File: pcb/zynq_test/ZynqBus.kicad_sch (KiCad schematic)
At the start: 22 parts, among them U1 XC7Z020-2CLG400I

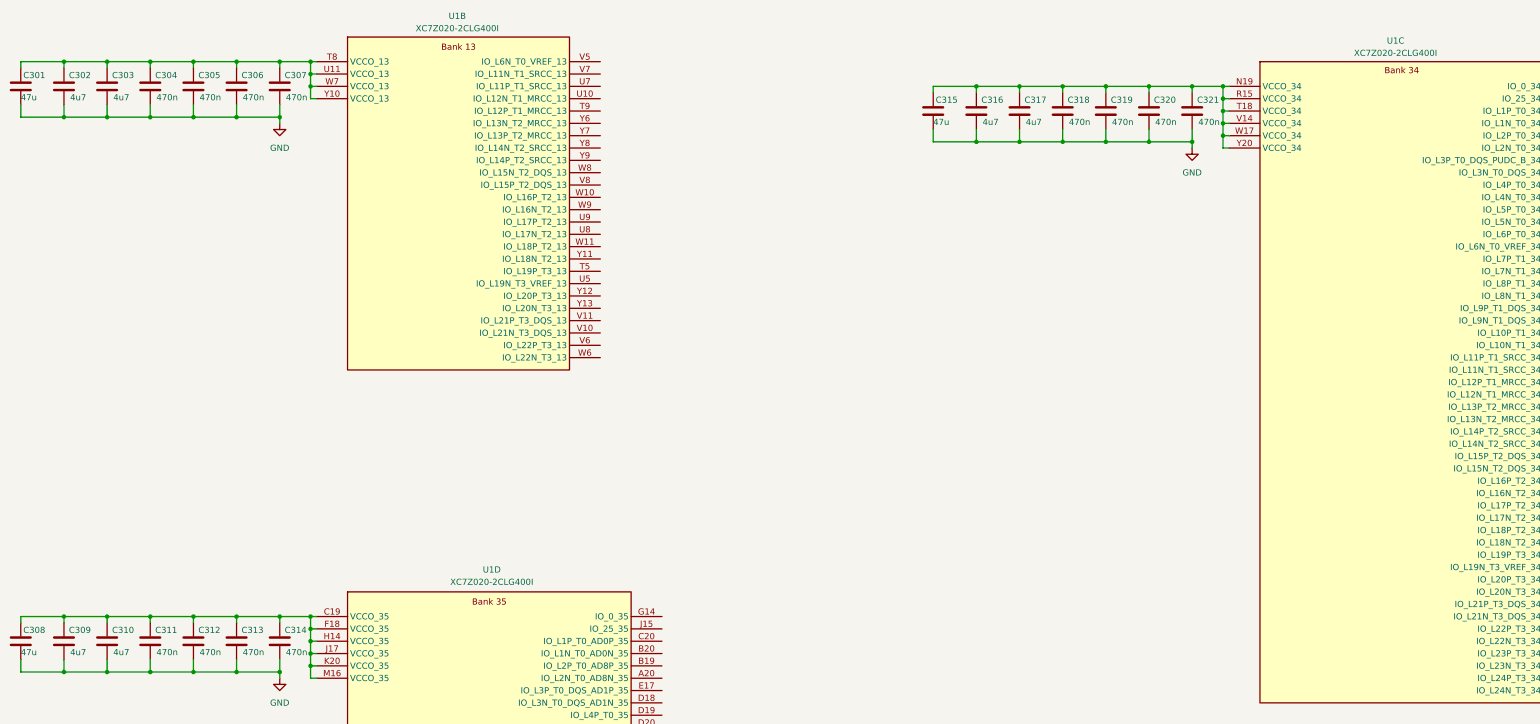
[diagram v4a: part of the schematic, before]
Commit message: Connected DDR3, cleaned up some thing
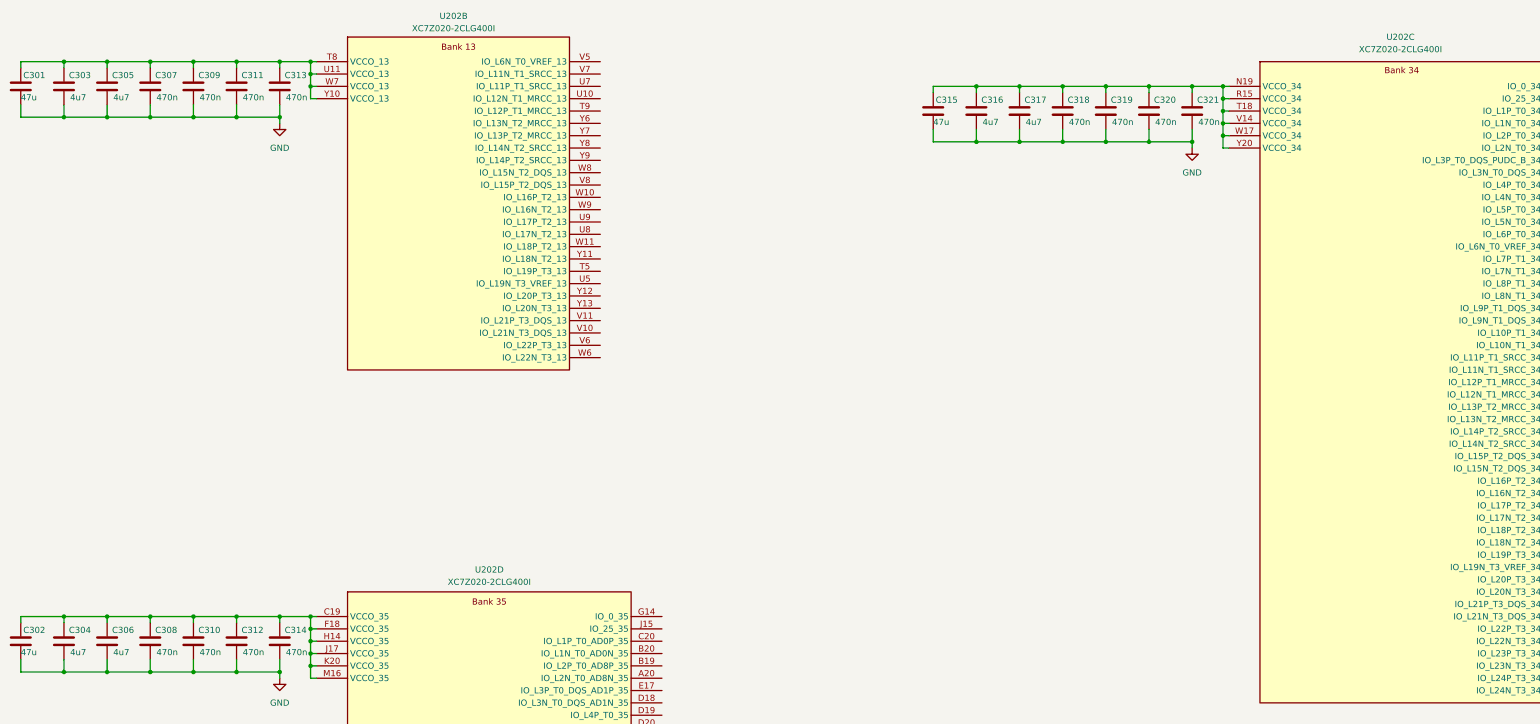
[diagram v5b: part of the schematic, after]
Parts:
- renumbered C308 to C302, C302 to C303, C309 to C304, C303 to C305, C310 to C306, C304 to C307, C311 to C308, C305 to C309, C312 to C310, C306 to C311, C313 to C312, C307 to C313, U1 to U202
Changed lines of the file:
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@@
 	(generator_version "9.0")
 	(paper "A3")
+	(title_block
+		(date "2025-09-06")
+		(rev "v1.0")
+	)
 	(junction
 		(at 240.03 44.45)
@@
 		(on_board yes)
 		(dnp no)
-		(property "Reference" "C313"
+		(property "Reference" "C312"
 			(at 61.976 145.034 0)
 			(effects
@@
 			(project "zynq_test"
 				(path "/0637578d-4ce5-4d31-b973-2de977269ea5/c459e1b5-5454-4a76-b5d2-e90b165c8789"
-					(reference "C313")
+					(reference "C312")
 					(unit 1)
 				)
@@
 		(on_board yes)
 		(dnp no)
-		(property "Reference" "C307"
+		(property "Reference" "C313"
 			(at 70.866 30.734 0)
 			(effects
@@
 			(project "zynq_test"
 				(path "/0637578d-4ce5-4d31-b973-2de977269ea5/c459e1b5-5454-4a76-b5d2-e90b165c8789"
-					(reference "C307")
+					(reference "C313")
 					(unit 1)
 				)
@@
 		(on_board yes)
 		(dnp no)
-		(property "Reference" "C303"
+		(property "Reference" "C305"
 			(at 35.306 30.734 0)
 			(effects
@@
 			(project "zynq_test"
 				(path "/0637578d-4ce5-4d31-b973-2de977269ea5/c459e1b5-5454-4a76-b5d2-e90b165c8789"
-					(reference "C303")
+					(reference "C305")
 					(unit 1)
 				)
@@
 	)
 	(symbol
-		(lib_name "XC7Z020-2CLG400I_2")
 		(lib_id "zynq:XC7Z020-2CLG400I")
 		(at 106.68 58.42 0)
@@
 		(on_board yes)
 		(dnp no)
-		(property "Reference" "U1"
-			(at 106.426 18.542 0)
+		(property "Reference" "U202"
+			(at 105.664 18.542 0)
 			(effects
 				(font
@@
 		)
 		(property "Value" "XC7Z020-2CLG400I"
-			(at 106.426 21.082 0)
+			(at 105.664 21.082 0)
 			(effects
 				(font
@@
 					(unit 2)
 				)
+				(path "/0637578d-4ce5-4d31-b973-2de977269ea5/920e1ce4-7460-4edb-8921-03ce78d5c203"
+					(reference "U202")
+					(unit 2)
+				)
 				(path "/0637578d-4ce5-4d31-b973-2de977269ea5/c459e1b5-5454-4a76-b5d2-e90b165c8789"
-					(reference "U1")
+					(reference "U202")
 					(unit 2)
 				)
@@
 		(on_board yes)
 		(dnp no)
-		(property "Reference" "C309"
+		(property "Reference" "C304"
 			(at 26.416 145.034 0)
 			(effects
@@
 			(project "zynq_test"
 				(path "/0637578d-4ce5-4d31-b973-2de977269ea5/c459e1b5-5454-4a76-b5d2-e90b165c8789"
-					(reference "C309")
+					(reference "C304")
 					(unit 1)
 				)
@@
 		(on_board yes)
 		(dnp no)
-		(property "Reference" "C308"
+		(property "Reference" "C302"
 			(at 17.018 145.034 0)
 			(effects
@@
 			(project "zynq_test"
 				(path "/0637578d-4ce5-4d31-b973-2de977269ea5/c459e1b5-5454-4a76-b5d2-e90b165c8789"
-					(reference "C308")
+					(reference "C302")
 					(unit 1)
 				)
@@
 		(on_board yes)
 		(dnp no)
-		(property "Reference" "C302"
+		(property "Reference" "C303"
 			(at 26.416 30.734 0)
 			(effects
@@
 			(project "zynq_test"
 				(path "/0637578d-4ce5-4d31-b973-2de977269ea5/c459e1b5-5454-4a76-b5d2-e90b165c8789"
-					(reference "C302")
+					(reference "C303")
 					(unit 1)
 				)
@@
 		(on_board yes)
 		(dnp no)
-		(property "Reference" "C304"
+		(property "Reference" "C307"
 			(at 44.196 30.734 0)
 			(effects
@@
 			(project "zynq_test"
 				(path "/0637578d-4ce5-4d31-b973-2de977269ea5/c459e1b5-5454-4a76-b5d2-e90b165c8789"
-					(reference "C304")
+					(reference "C307")
 					(unit 1)
 				)
@@
 		(on_board yes)
 		(dnp no)
-		(property "Reference" "C305"
+		(property "Reference" "C309"
 			(at 53.086 30.734 0)
 			(effects
@@
 			(project "zynq_test"
 				(path "/0637578d-4ce5-4d31-b973-2de977269ea5/c459e1b5-5454-4a76-b5d2-e90b165c8789"
-					(reference "C305")
+					(reference "C309")
 					(unit 1)
 				)
@@
 		(on_board yes)
 		(dnp no)
-		(property "Reference" "C311"
+		(property "Reference" "C308"
 			(at 44.196 145.034 0)
 			(effects
@@
 			(project "zynq_test"
 				(path "/0637578d-4ce5-4d31-b973-2de977269ea5/c459e1b5-5454-4a76-b5d2-e90b165c8789"
-					(reference "C311")
+					(reference "C308")
 					(unit 1)
 				)
@@
 		(on_board yes)
 		(dnp no)
-		(property "Reference" "C310"
+		(property "Reference" "C306"
 			(at 35.306 145.034 0)
 			(effects
@@
 			(project "zynq_test"
 				(path "/0637578d-4ce5-4d31-b973-2de977269ea5/c459e1b5-5454-4a76-b5d2-e90b165c8789"
-					(reference "C310")
+					(reference "C306")
 					(unit 1)
 				)
@@
 		(on_board yes)
 		(dnp no)
-		(property "Reference" "U1"
-			(at 113.538 132.588 0)
+		(property "Reference" "U202"
+			(at 113.03 132.588 0)
 			(effects
 				(font
@@
 		)
 		(property "Value" "XC7Z020-2CLG400I"
-			(at 113.538 135.128 0)
+			(at 113.03 135.128 0)
 			(effects
 				(font
@@
 					(unit 4)
 				)
+				(path "/0637578d-4ce5-4d31-b973-2de977269ea5/920e1ce4-7460-4edb-8921-03ce78d5c203"
+					(reference "U202")
+					(unit 4)
+				)
 				(path "/0637578d-4ce5-4d31-b973-2de977269ea5/c459e1b5-5454-4a76-b5d2-e90b165c8789"
-					(reference "U1")
+					(reference "U202")
 					(unit 4)
 				)
@@
 		(on_board yes)
 		(dnp no)
-		(property "Reference" "C312"
+		(property "Reference" "C310"
 			(at 53.086 145.034 0)
 			(effects
@@
 			(project "zynq_test"
 				(path "/0637578d-4ce5-4d31-b973-2de977269ea5/c459e1b5-5454-4a76-b5d2-e90b165c8789"
-					(reference "C312")
+					(reference "C310")
 					(unit 1)
 				)
@@
 	)
 	(symbol
-		(lib_name "XC7Z020-2CLG400I_1")
 		(lib_id "zynq:XC7Z020-2CLG400I")
 		(at 300.99 93.98 0)
@@
 		(on_board yes)
 		(dnp no)
-		(property "Reference" "U1"
-			(at 299.72 23.622 0)
+		(property "Reference" "U202"
+			(at 300.736 22.86 0)
 			(effects
 				(font
@@
 		)
 		(property "Value" "XC7Z020-2CLG400I"
-			(at 299.72 26.162 0)
+			(at 300.736 25.4 0)
 			(effects
 				(font
@@
 					(unit 3)
 				)
+				(path "/0637578d-4ce5-4d31-b973-2de977269ea5/920e1ce4-7460-4edb-8921-03ce78d5c203"
+					(reference "U202")
+					(unit 3)
+				)
 				(path "/0637578d-4ce5-4d31-b973-2de977269ea5/c459e1b5-5454-4a76-b5d2-e90b165c8789"
-					(reference "U1")
+					(reference "U202")
 					(unit 3)
 				)
@@
 		(on_board yes)
 		(dnp no)
-		(property "Reference" "C306"
+		(property "Reference" "C311"
 			(at 61.976 30.734 0)
 			(effects
@@
 			(project "zynq_test"
 				(path "/0637578d-4ce5-4d31-b973-2de977269ea5/c459e1b5-5454-4a76-b5d2-e90b165c8789"
-					(reference "C306")
+					(reference "C311")
 					(unit 1)
 				)

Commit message: Finished Power Supply
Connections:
- net +3V3: now reaches C302.1, C304.1, C306.1, C308.1, C310.1, C312.1, C314.1, U202.C19 (VCCO_35), U202.F18 (VCCO_35), U202.H14 (VCCO_35), U202.J17 (VCCO_35), U202.K20 (VCCO_35), U202.M16 (VCCO_35)
- net +3V3: now also C301.1, C303.1, C305.1, C307.1, C309.1, C311.1, C313.1, C315.1, C316.1, C317.1, C318.1, C319.1, C320.1, C321.1, U202.N19 (VCCO_34), U202.R15 (VCCO_34), U202.T18 (VCCO_34), U202.T8 (VCCO_13), U202.U11 (VCCO_13), U202.V14 (VCCO_34), U202.W17 (VCCO_34), U202.W7 (VCCO_13), U202.Y10 (VCCO_13), U202.Y20 (VCCO_34)
- no-connect marks 0 -> 125
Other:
- title: (none) -> Zynq FPGA IO

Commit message: Finished most of the schematic, will start routing soon
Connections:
- net +3V3: no longer C301.1, C303.1, C305.1, C307.1, C309.1, C311.1, C313.1, U202.T8 (VCCO_13), U202.U11 (VCCO_13), U202.W7 (VCCO_13), U202.Y10 (VCCO_13)
- net GPIO0.17: now reaches U202.T5 (IO_L19P_T3_13)
- net GPIO0.4: now reaches U202.T9 (IO_L12P_T1_MRCC_13)
- net GPIO0.3: now reaches U202.U10 (IO_L12N_T1_MRCC_13)
- net GPIO0.18: now reaches U202.U5 (IO_L19N_T3_VREF_13)
- net GPIO0.2: now reaches U202.U7 (IO_L11P_T1_SRCC_13)
- net GPIO0.14: now reaches U202.U8 (IO_L17N_T2_13)
- net GPIO0.13: now reaches U202.U9 (IO_L17P_T2_13)
- net GPIO0.22: now reaches U202.V10 (IO_L21N_T3_DQS_13)
- net GPIO0.21: now reaches U202.V11 (IO_L21P_T3_DQS_13)
- net GPIO0.0: now reaches U202.V5 (IO_L6N_T0_VREF_13)
- net GPIO0.23: now reaches U202.V6 (IO_L22P_T3_13)
- net GPIO0.1: now reaches U202.V7 (IO_L11N_T1_SRCC_13)
- net GPIO0.10: now reaches U202.V8 (IO_L15P_T2_DQS_13)
- net GPIO0.11: now reaches U202.W10 (IO_L16P_T2_13)
- net GPIO0.15: now reaches U202.W11 (IO_L18P_T2_13)
- net GPIO0.24: now reaches U202.W6 (IO_L22N_T3_13)
- net GPIO0.9: now reaches U202.W8 (IO_L15N_T2_DQS_13)
- net GPIO0.12: now reaches U202.W9 (IO_L16N_T2_13)
- net GPIO0.16: now reaches U202.Y11 (IO_L18N_T2_13)
- net GPIO0.19: now reaches U202.Y12 (IO_L20P_T3_13)
- net GPIO0.20: now reaches U202.Y13 (IO_L20N_T3_13)
- net GPIO0.5: now reaches U202.Y6 (IO_L13N_T2_MRCC_13)
- net GPIO0.6: now reaches U202.Y7 (IO_L13P_T2_MRCC_13)
- net GPIO0.7: now reaches U202.Y8 (IO_L14N_T2_SRCC_13)
- net GPIO0.8: now reaches U202.Y9 (IO_L14P_T2_SRCC_13)
- net HDMI.TX.D2_N: now reaches U202.A20 (IO_L2N_T0_AD8N_35)
- net HDMI.TX.D2_P: now reaches U202.B19 (IO_L2P_T0_AD8P_35)
- net HDMI.TX.D1_N: now reaches U202.B20 (IO_L1N_T0_AD0N_35)
- net HDMI.TX.D1_P: now reaches U202.C20 (IO_L1P_T0_AD0P_35)
- net HDMI.RX.D2_N: now reaches U202.D18 (IO_L3N_T0_DQS_AD1N_35)
- net HDMI.TX.D0_P: now reaches U202.D19 (IO_L4P_T0_35)
- net HDMI.TX.D0_N: now reaches U202.D20 (IO_L4N_T0_35)
- net HDMI.RX.D2_P: now reaches U202.E17 (IO_L3P_T0_DQS_AD1P_35)
- net HDMI.TX.CLK_P: now reaches U202.E18 (IO_L5P_T0_AD9P_35)
- net HDMI.TX.CLK_N: now reaches U202.E19 (IO_L5N_T0_AD9N_35)
- net HDMI.RX.D1_P: now reaches U202.F16 (IO_L6P_T0_35)
- net HDMI.RX.D1_N: now reaches U202.F17 (IO_L6N_T0_VREF_35)
- net CAM_RX.0.CAM_D0_P: now reaches U202.F19 (IO_L15P_T2_DQS_AD12P_35)
- net CAM_RX.0.CAM_D0_N: now reaches U202.F20 (IO_L15N_T2_DQS_AD12N_35)
- net HDMI.TX.SCL: now reaches U202.G14 (IO_0_35)
- net HDMI.RX.D0_N: now reaches U202.G15 (IO_L19N_T3_VREF_35)
- net HDMI.RX.CLK_P: now reaches U202.G17 (IO_L16P_T2_35)
- net HDMI.RX.CLK_N: now reaches U202.G18 (IO_L16N_T2_35)
- net CAM_RX.0.LN_0_P: now reaches U202.G19 (IO_L18P_T2_AD13P_35)
- net CAM_RX.0.LN_0_N: now reaches U202.G20 (IO_L18N_T2_AD13N_35)
- net HDMI.RX.D0_P: now reaches U202.H15 (IO_L19P_T3_35)
- net CLK_125M: now reaches U202.H16 (IO_L13P_T2_MRCC_35)
- net HDMI.RX.SDA: now reaches U202.H18 (IO_L14N_T2_AD4N_SRCC_35)
- net CAM_RX.0.CAM_D1_N: now reaches U202.H20 (IO_L17N_T2_AD5N_35)
- net HDMI.TX.HDP: now reaches U202.J14 (IO_L20N_T3_AD6N_35)
- net HDMI.TX.SDA: now reaches U202.J15 (IO_25_35)
- net HDMI.CTR.SCL: now reaches U202.J16 (IO_L24N_T3_AD15N_35)
- net HDMI.RX.SCL: now reaches U202.J18 (IO_L14P_T2_AD4P_SRCC_35)
- net CAM_RX.0.LN_1_N: now reaches U202.J19 (IO_L10N_T1_AD11N_35)
- net CAM_RX.0.CAM_D1_P: now reaches U202.J20 (IO_L17P_T2_AD5P_35)
- net ETH0_INT: now reaches U202.K14 (IO_L20P_T3_AD6P_35)
- net HDMI.CTR.SDA: now reaches U202.K16 (IO_L24P_T3_AD15P_35)
- net CAM_RX.0.I2C_CLK: now reaches U202.K17 (IO_L12P_T1_MRCC_35)
- net CAM_RX.0.I2C_SDA: now reaches U202.K18 (IO_L12N_T1_MRCC_35)
- net CAM_RX.0.LN_1_P: now reaches U202.K19 (IO_L10P_T1_AD11P_35)
- net ETH0_RST: now reaches U202.L14 (IO_L22P_T3_AD7P_35)
- net HDMI.EN: now reaches U202.L16 (IO_L11P_T1_SRCC_35)
- net CAM_RX.0.CAM_CLK_P: now reaches U202.L19 (IO_L9P_T1_DQS_AD3P_35)
- net CAM_RX.0.CAM_CLK_N: now reaches U202.L20 (IO_L9N_T1_DQS_AD3N_35)
- net CAM_RX.0.LN_CLK_P: now reaches U202.M19 (IO_L7P_T1_AD2P_35)
- net CAM_RX.0.LN_CLK_N: now reaches U202.M20 (IO_L7N_T1_AD2N_35)
- net GPIO2.8: now reaches U202.N17 (IO_L23P_T3_34)
- net GPIO2.2: now reaches U202.N18 (IO_L13P_T2_MRCC_34)
- net GPIO2.4: now reaches U202.N20 (IO_L14P_T2_SRCC_34)
- net GPIO1.8: now reaches U202.P14 (IO_L6P_T0_34)
- net CAM_TX.2.LN_0_P: now reaches U202.P15 (IO_L24P_T3_34)
- net CAM_TX.2.LN_0_N: now reaches U202.P16 (IO_L24N_T3_34)
- net GPIO2.9: now reaches U202.P18 (IO_L23N_T3_34)
- net GPIO2.3: now reaches U202.P19 (IO_L13N_T2_MRCC_34)
- net GPIO2.5: now reaches U202.P20 (IO_L14N_T2_SRCC_34)
- net GPIO1.9: now reaches U202.R14 (IO_L6N_T0_VREF_34)
- net CAM_TX.2.CAM_D0_P: now reaches U202.R16 (IO_L19P_T3_34)
- net CAM_TX.2.CAM_D0_N: now reaches U202.R17 (IO_L19N_T3_VREF_34)
- net CAM_TX.2.LN_1_N: now reaches U202.R18 (IO_L20N_T3_34)
- net GPIO2.0: now reaches U202.R19 (IO_0_34)
- net GPIO1.1: now reaches U202.T10 (IO_L1N_T0_34)
- net GPIO1.0: now reaches U202.T11 (IO_L1P_T0_34)
- net GPIO1.2: now reaches U202.T12 (IO_L2P_T0_34)
- net CAM_TX.2.I2C_CLK: now reaches U202.T14 (IO_L5P_T0_34)
- net CAM_TX.2.I2C_SDA: now reaches U202.T15 (IO_L5N_T0_34)
- net CAM_TX.2.LN_CLK_P: now reaches U202.T16 (IO_L9P_T1_DQS_34)
- net CAM_TX.2.LN_1_P: now reaches U202.T17 (IO_L20P_T3_34)
- net GPIO2.1: now reaches U202.T19 (IO_25_34)
- net GPIO2.6: now reaches U202.T20 (IO_L15P_T2_DQS_34)
- net GPIO1.3: now reaches U202.U12 (IO_L2N_T0_34)
- net GPIO1.4: now reaches U202.U13 (IO_L3P_T0_DQS_PUDC_B_34)
- net GPIO1.10: now reaches U202.U14 (IO_L11P_T1_SRCC_34)
- net GPIO1.11: now reaches U202.U15 (IO_L11N_T1_SRCC_34)
- net CAM_TX.2.LN_CLK_N: now reaches U202.U17 (IO_L9N_T1_DQS_34)
- net CAM_TX.2.CAM_D1_P: now reaches U202.U18 (IO_L12P_T1_MRCC_34)
- net CAM_TX.2.CAM_D1_N: now reaches U202.U19 (IO_L12N_T1_MRCC_34)
- net GPIO2.7: now reaches U202.U20 (IO_L15N_T2_DQS_34)
- net GPIO1.6: now reaches U202.V12 (IO_L4P_T0_34)
- net GPIO1.5: now reaches U202.V13 (IO_L3N_T0_DQS_34)
- net CAM_RX.1.CAM_CLK_P: now reaches U202.V15 (IO_L10P_T1_34)
- net CAM_RX.1.LN_1_P: now reaches U202.V16 (IO_L18P_T2_34)
- net CAM_TX.2.CAM_CLK_P: now reaches U202.V17 (IO_L21P_T3_DQS_34)
- net CAM_TX.2.CAM_CLK_N: now reaches U202.V18 (IO_L21N_T3_DQS_34)
- net CAM_RX.1.I2C_CLK: now reaches U202.V20 (IO_L16P_T2_34)
- net GPIO1.7: now reaches U202.W13 (IO_L4N_T0_34)
- net CAM_RX.1.LN_CLK_P: now reaches U202.W14 (IO_L8P_T1_34)
- net CAM_RX.1.CAM_CLK_N: now reaches U202.W15 (IO_L10N_T1_34)
- net CAM_RX.1.LN_1_N: now reaches U202.W16 (IO_L18N_T2_34)
- net CAM_RX.1.LN_0_P: now reaches U202.W18 (IO_L22P_T3_34)
- net CAM_RX.1.LN_0_N: now reaches U202.W19 (IO_L22N_T3_34)
- net CAM_RX.1.I2C_SDA: now reaches U202.W20 (IO_L16N_T2_34)
- net CAM_RX.1.LN_CLK_N: now reaches U202.Y14 (IO_L8N_T1_34)
- net CAM_RX.1.CAM_D1_P: now reaches U202.Y16 (IO_L7P_T1_34)
- net CAM_RX.1.CAM_D1_N: now reaches U202.Y17 (IO_L7N_T1_34)
- net CAM_RX.1.CAM_D0_P: now reaches U202.Y18 (IO_L17P_T2_34)
- net CAM_RX.1.CAM_D0_N: now reaches U202.Y19 (IO_L17N_T2_34)
- new net +1V8: C301.1, C303.1, C305.1, C307.1, C309.1, C311.1, C313.1, U202.T8 (VCCO_13), U202.U11 (VCCO_13), U202.W7 (VCCO_13), U202.Y10 (VCCO_13)
- no-connect marks 125 -> 9
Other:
- moved on the sheet: C302, C304, C306, C308, C310, C312, C314, C315, C316, C317, C318, C319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

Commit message: Finished to first ddr ic
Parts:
- U202: footprint Package_BGA:Xilinx_CLG400 -> Zynq:Zynq_Z7020-2CLG400I_W_Delay
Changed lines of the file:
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@@
 			)
 		)
-		(property "Footprint" "Package_BGA:Xilinx_CLG400"
+		(property "Footprint" "Zynq:Zynq_Z7020-2CLG400I_W_Delay"
 			(at 77.47 -17.78 0)
 			(effects
@@
 			)
 		)
-		(property "Footprint" "Package_BGA:Xilinx_CLG400"
+		(property "Footprint" "Zynq:Zynq_Z7020-2CLG400I_W_Delay"
 			(at 82.55 132.08 0)
 			(effects
@@
 			)
 		)
-		(property "Footprint" "Package_BGA:Xilinx_CLG400"
+		(property "Footprint" "Zynq:Zynq_Z7020-2CLG400I_W_Delay"
 			(at 284.48 81.28 0)
 			(effects
